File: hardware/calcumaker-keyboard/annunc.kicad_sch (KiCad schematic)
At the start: 10 parts

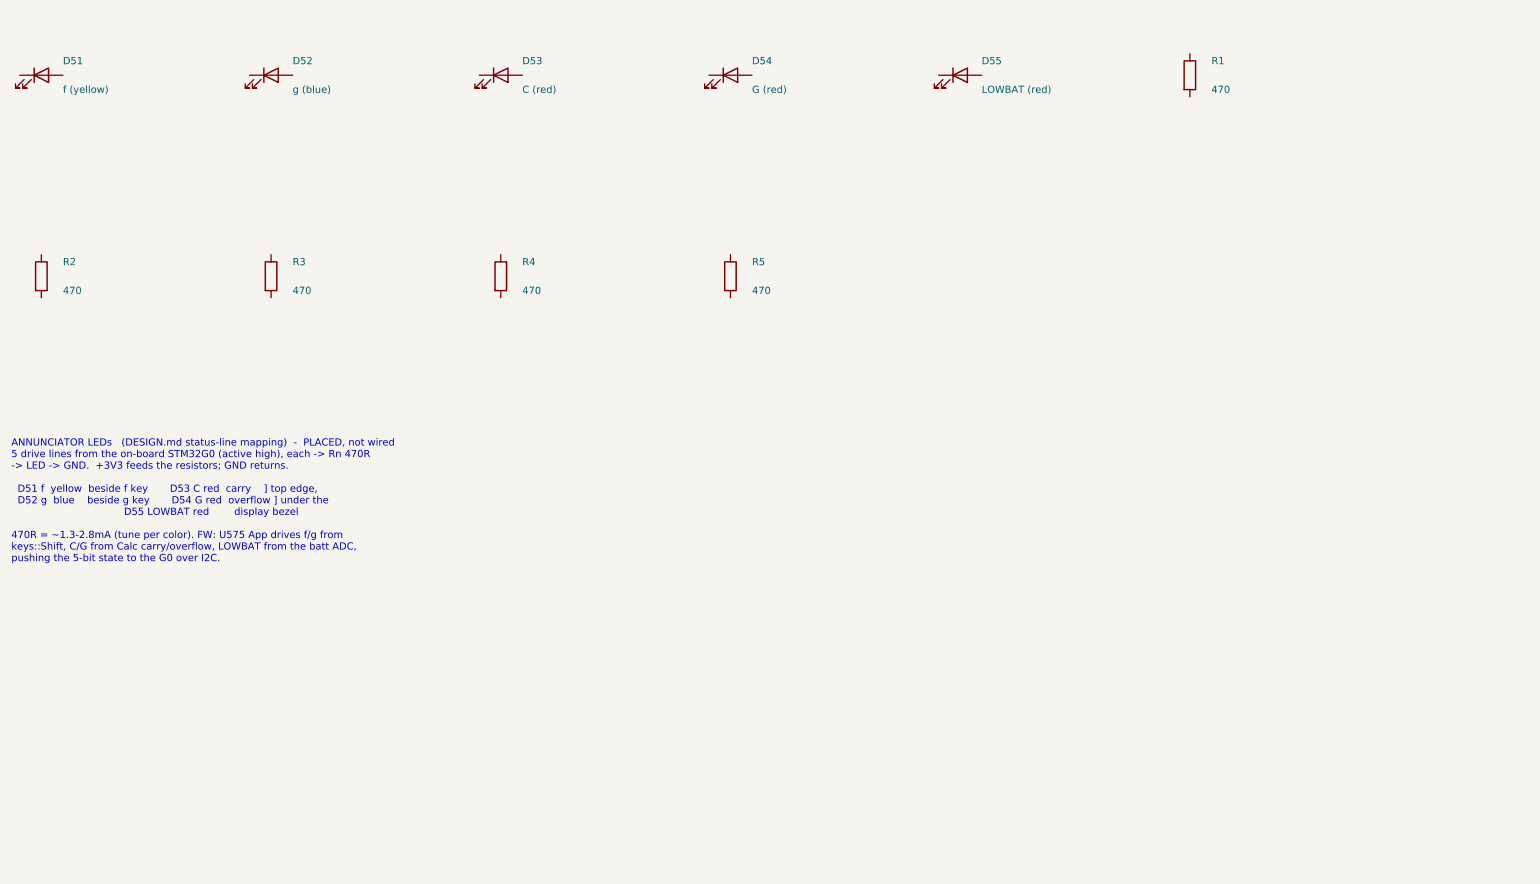
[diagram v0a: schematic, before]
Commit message: Wire mainboard and keypad schematics and verify expanded nets
Connect hierarchical interfaces, power/control circuits, debug links, matrix and RGB chains. Correct MCU package pins, diode polarity and power configuration; add bypass components and repeatable KiCad netlist/ERC checks. Document pin maps and remaining physical validation.
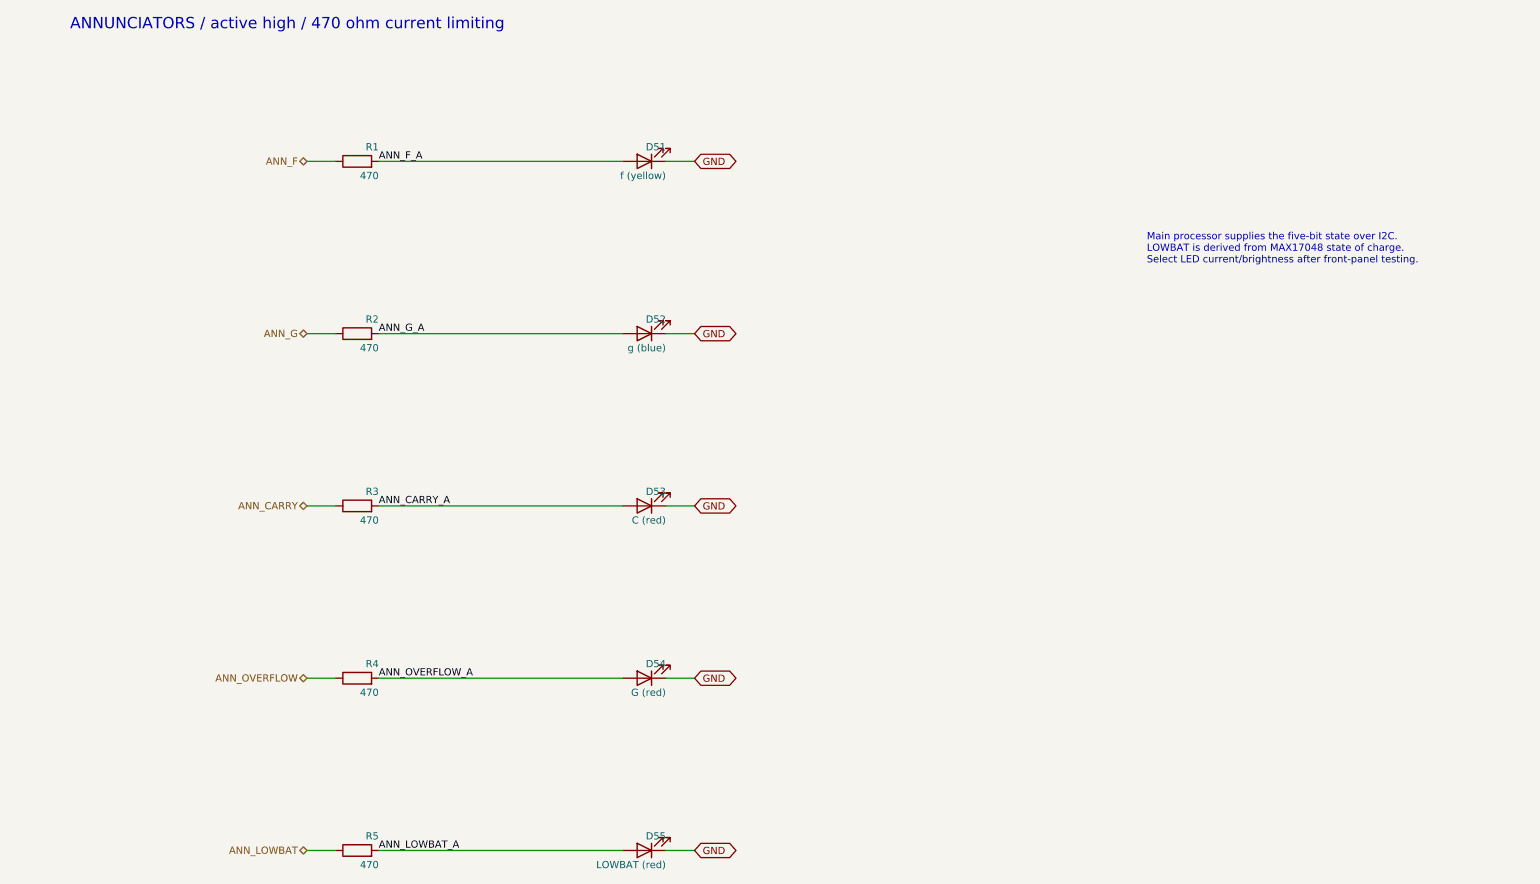
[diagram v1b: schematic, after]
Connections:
- net GND: now reaches D55.1 (K)
- net GND: now also D51.1 (K), D52.1 (K), D53.1 (K), D54.1 (K)
- net ANN_LOWBAT_A: now reaches D55.2 (A)
- net ANN_LOWBAT_A: now also R5.2
- net ANN_F: now reaches R1.1
- net ANN_F_A: now reaches R1.2
- net ANN_F_A: now also D51.2 (A)
- net ANN_CARRY_A: now reaches D53.2 (A)
- net ANN_CARRY_A: now also R3.2
- net ANN_OVERFLOW: now reaches R4.1
- net ANN_OVERFLOW_A: now reaches R4.2
- net ANN_OVERFLOW_A: now also D54.2 (A)
- net ANN_LOWBAT: now reaches R5.1
- net ANN_G_A: now reaches D52.2 (A)
- net ANN_G_A: now also R2.2
- net ANN_CARRY: now reaches R3.1
- net ANN_G: now reaches R2.1
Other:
- note added: "ANNUNCIATORS / active high / 470 ohm current limiting"
- note added: "Main processor supplies the five-bit state over I2C. LOWBAT is derived from MAX17048 state of charge. Select LED current/brightness after front-panel testing."
- note removed: "ANNUNCIATOR LEDs (DESIGN.md status-line mapping) - PLACED, not wired 5 drive lines from the on-board STM32G0 (active high), each -> Rn 470R -> LED -> GND. +3V3 feeds the resistors; GND returns. D51 f yellow beside f key D53 C red carry ] top edge, D52 g blue beside g key D54 G red overflow ] under the D55 LOWBAT red display bezel 470R = ~1.3-2.8mA (tune per color). FW: U575 App drives f/g from ke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"
- title: Calcumaker 16 — Keyboard — Annunciator LEDs (f g C G low-batt) -> Calcumaker 16 / keyboard / annunc
- moved on the sheet: D51, D52, D53, D54, D55, R1, R2, R3, R4, R5
